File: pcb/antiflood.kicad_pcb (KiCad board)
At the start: 2 copper layers, 88 x 84 mm, 98 parts, among them J1 Barrel_Jack, J10 Screw_Terminal_01x02, J11 Screw_Terminal_01x02, J12 Screw_Terminal_01x02, J13 Screw_Terminal_01x02, J2 Conn_01x03_Male, J3 01x03, J4 01x03, J5 Conn_02x04_Odd_Even, J6 Conn_02x05_Odd_Even, J7 Conn_02x03_Odd_Even, J8 Screw_Terminal_01x02, J9 Screw_Terminal_01x02, K1 P-5, K2 P-5, Q1 MMBT3904, Q2 MMBT3904, SW1 SW_Push, SW2 SW_Push, SW3 SW_Push, U1 ATMEGA328P-AU, U2 TL7705, U3 LM1117-3.3, U4 MT3608, U5 MC34063, U6 TP4056, Y1 16MHz

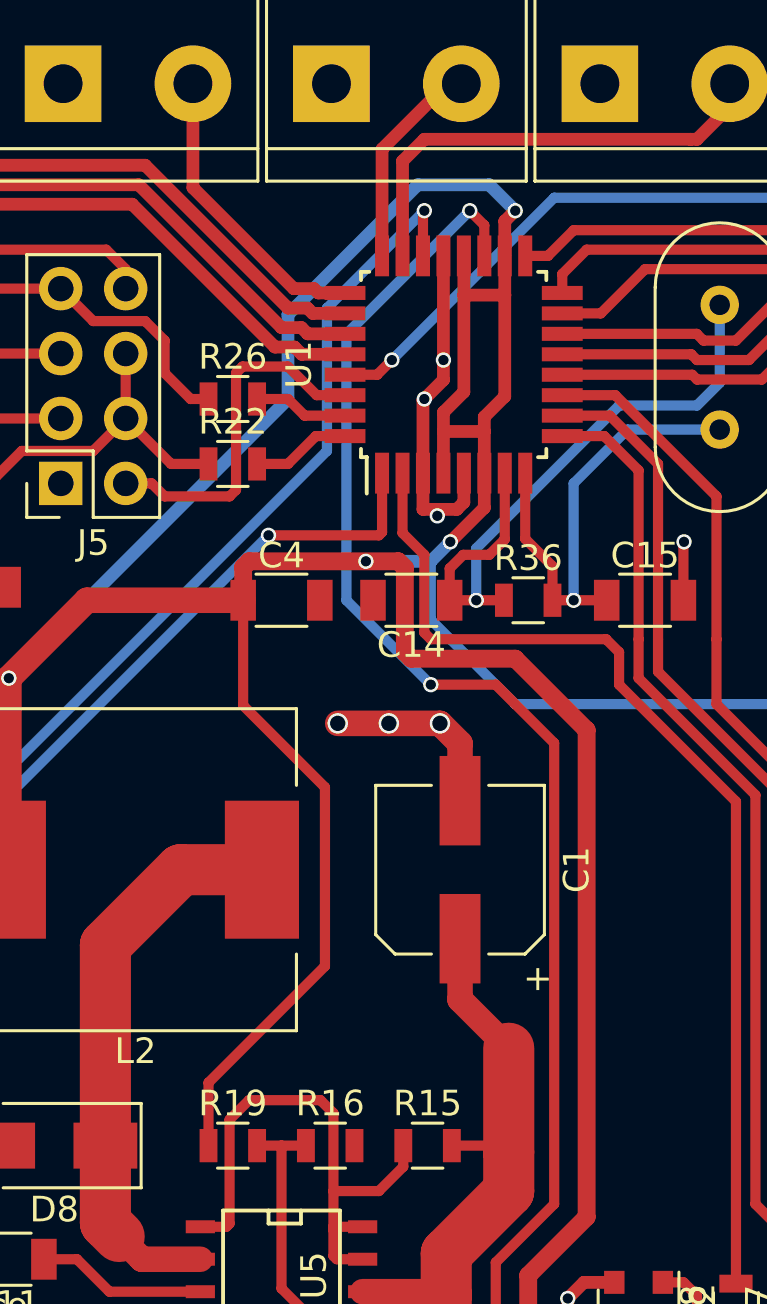
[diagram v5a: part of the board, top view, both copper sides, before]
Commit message: PCB: filled zones
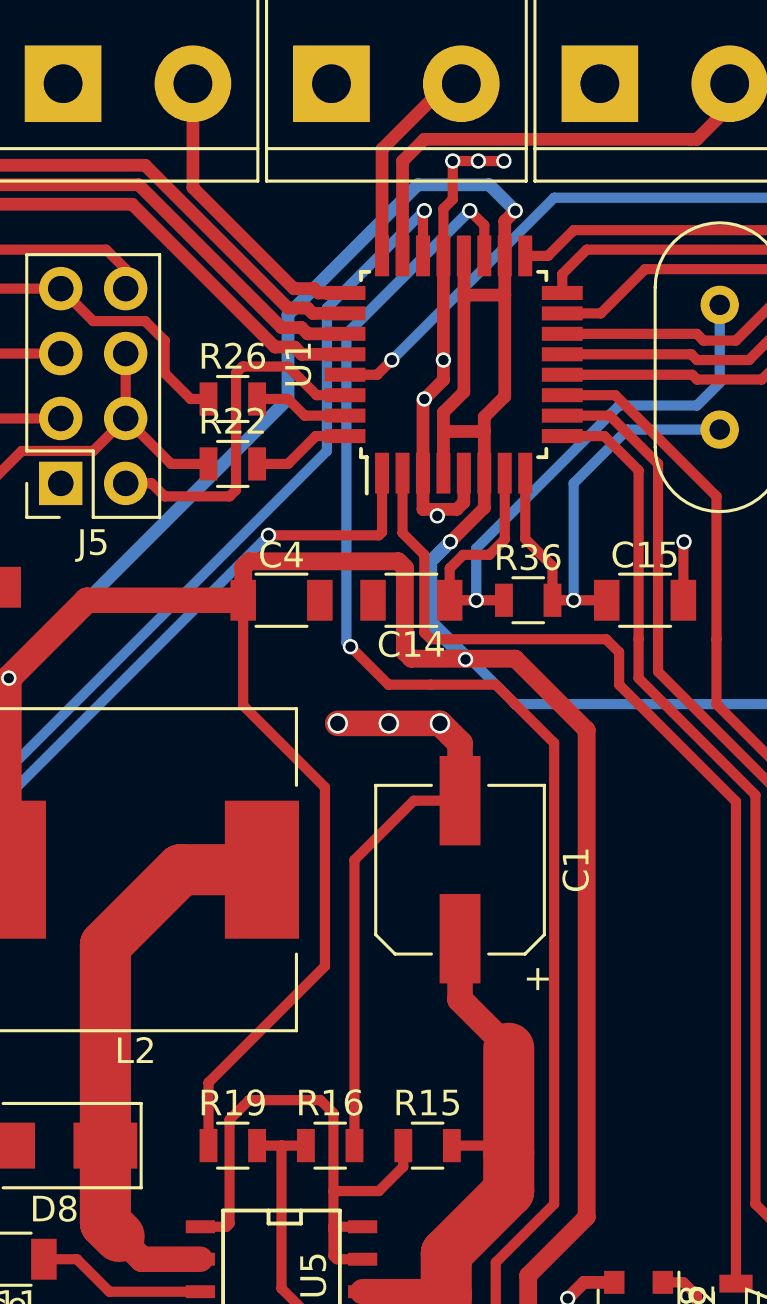
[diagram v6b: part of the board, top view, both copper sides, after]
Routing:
- net GND: track 101.8 -> 123.9 mm, vias 44 -> 47
- net /A6: track 151.7 -> 159.5 mm
- net +5V: track 364.9 -> 363.4 mm
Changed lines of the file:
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@@
   (general
     (links 217)
-    (no_connects 61)
+    (no_connects 0)
     (area 71.454999 50.924999 159.555001 135.025001)
     (thickness 1.6)
     (drawings 24)
-    (tracks 826)
+    (tracks 845)
     (zones 0)
     (modules 98)
@@
     (pad_to_mask_clearance 0)
     (aux_axis_origin 71.505 50.975)
-    (visible_elements FFFEFF7F)
+    (visible_elements FFFEF77F)
     (pcbplotparams
       (layerselection 0x00030_80000001)
@@
   (gr_line (start 159.505 50.975) (end 159.505 134.975) (angle 90) (layer Edge.Cuts) (width 0.1))
   (gr_line (start 71.505 50.975) (end 159.505 50.975) (angle 90) (layer Edge.Cuts) (width 0.1))
+  (segment (start 117.155 96.52) (end 117.155 85.345) (width 0.4) (layer F.Cu) (net 1) (status 400000))
+  (segment (start 119.475 83.025) (end 121.285 83.025) (width 0.4) (layer F.Cu) (net 1) (status 800000))
+  (segment (start 117.155 85.345) (end 119.475 83.025) (width 0.4) (layer F.Cu) (net 1))
+  (segment (start 122 58) (end 123 58) (width 0.4) (layer F.Cu) (net 1))
+  (via (at 123 58) (size 0.6) (drill 0.4) (layers F.Cu B.Cu) (net 1))
+  (segment (start 121 58) (end 122 58) (width 0.4) (layer F.Cu) (net 1))
+  (via (at 122 58) (size 0.6) (drill 0.4) (layers F.Cu B.Cu) (net 1))
+  (segment (start 121 59.5) (end 121 58) (width 0.4) (layer F.Cu) (net 1))
+  (via (at 121 58) (size 0.6) (drill 0.4) (layers F.Cu B.Cu) (net 1))
+  (segment (start 120.635 61.711) (end 120.635 59.865) (width 0.4) (layer F.Cu) (net 1))
+  (segment (start 120.635 59.865) (end 121 59.5) (width 0.4) (layer F.Cu) (net 1))
   (segment (start 100.5 131) (end 100.5 129.5) (width 0.4) (layer F.Cu) (net 1))
   (via (at 100.5 129.5) (size 0.6) (drill 0.4) (layers F.Cu B.Cu) (net 1))
   (segment (start 100.5 132.5) (end 100.5 131) (width 0.4) (layer F.Cu) (net 1))
   (via (at 100.5 131) (size 0.6) (drill 0.4) (layers F.Cu B.Cu) (net 1))
-  (segment (start 102.87 133.095) (end 101.095 133.095) (width 0.4) (layer F.Cu) (net 1) (status 400000))
+  (segment (start 102.87 133.095) (end 101.095 133.095) (width 0.4) (layer F.Cu) (net 1))
   (segment (start 101.095 133.095) (end 100.5 132.5) (width 0.4) (layer F.Cu) (net 1))
   (via (at 100.5 132.5) (size 0.6) (drill 0.4) (layers F.Cu B.Cu) (net 1))
-  (segment (start 84.455 99.06) (end 84.455 98.455) (width 0.5) (layer F.Cu) (net 1) (status 400000))
+  (segment (start 84.455 99.06) (end 84.455 98.455) (width 0.5) (layer F.Cu) (net 1))
   (segment (start 84.455 98.455) (end 83.5 97.5) (width 0.5) (layer F.Cu) (net 1))
   (via (at 83.5 97.5) (size 0.6) (drill 0.4) (layers F.Cu B.Cu) (net 1))
-  (segment (start 76.2 99.06) (end 76.2 98.2) (width 0.5) (layer F.Cu) (net 1) (status 400000))
+  (segment (start 76.2 99.06) (end 76.2 98.2) (width 0.5) (layer F.Cu) (net 1))
   (segment (start 76.2 98.2) (end 75.5 97.5) (width 0.5) (layer F.Cu) (net 1))
   (via (at 75.5 97.5) (size 0.6) (drill 0.4) (layers F.Cu B.Cu) (net 1))
@@
   (segment (start 150.5 104.5) (end 150.5 102.5) (width 1) (layer F.Cu) (net 1))
   (via (at 150.5 102.5) (size 0.8) (drill 0.6) (layers F.Cu B.Cu) (net 1))
-  (segment (start 150.495 106.77) (end 150.495 104.505) (width 1) (layer F.Cu) (net 1) (status 400000))
+  (segment (start 150.495 106.77) (end 150.495 104.505) (width 1) (layer F.Cu) (net 1))
   (segment (start 150.495 104.505) (end 150.5 104.5) (width 1) (layer F.Cu) (net 1))
   (via (at 150.5 104.5) (size 0.8) (drill 0.6) (layers F.Cu B.Cu) (net 1))
@@
   (segment (start 155.5 104.5) (end 155.5 102.5) (width 1) (layer F.Cu) (net 1))
   (via (at 155.5 102.5) (size 0.8) (drill 0.6) (layers F.Cu B.Cu) (net 1))
-  (segment (start 155.575 106.77) (end 155.575 104.575) (width 1) (layer F.Cu) (net 1) (status 400000))
+  (segment (start 155.575 106.77) (end 155.575 104.575) (width 1) (layer F.Cu) (net 1))
   (segment (start 155.575 104.575) (end 155.5 104.5) (width 1) (layer F.Cu) (net 1))
   (via (at 155.5 104.5) (size 0.8) (drill 0.6) (layers F.Cu B.Cu) (net 1))
@@
   (segment (start 109.5 103.5) (end 107.5 103.5) (width 1) (layer F.Cu) (net 1))
   (via (at 107.5 103.5) (size 0.8) (drill 0.6) (layers F.Cu B.Cu) (net 1))
-  (segment (start 111.125 103.505) (end 109.505 103.505) (width 1) (layer F.Cu) (net 1) (status 400000))
+  (segment (start 111.125 103.505) (end 109.505 103.505) (width 1) (layer F.Cu) (net 1))
   (segment (start 109.505 103.505) (end 109.5 103.5) (width 1) (layer F.Cu) (net 1))
   (via (at 109.5 103.5) (size 0.8) (drill 0.6) (layers F.Cu B.Cu) (net 1))
@@
   (segment (start 124.079 121.285) (end 126.365 121.285) (width 2) (layer F.Cu) (net 2))
   (segment (start 120.745 117.951) (end 124.079 121.285) (width 2) (layer F.Cu) (net 2))
+  (segment (start 120.904 72.898) (end 120.142 73.66) (width 0.5) (layer B.Cu) (net 3))
+  (segment (start 120.142 73.66) (end 120.142 76.142) (width 0.5) (layer B.Cu) (net 3))
+  (segment (start 120.142 76.142) (end 121.5 77.5) (width 0.5) (layer B.Cu) (net 3))
+  (via (at 121.5 77.5) (size 0.6) (drill 0.4) (layers F.Cu B.Cu) (net 3))
+  (segment (start 121.5 77.5) (end 121.5 77.47) (width 0.5) (layer F.Cu) (net 3))
+  (segment (start 121.5 77.47) (end 121.5 77.5) (width 0.5) (layer F.Cu) (net 3))
+  (segment (start 121.5 77.5) (end 121.5 77.47) (width 0.5) (layer F.Cu) (net 3))
   (segment (start 112.8 75.184) (end 112.8 79.3) (width 0.4) (layer F.Cu) (net 3))
   (segment (start 112.8 79.3) (end 116 82.5) (width 0.4) (layer F.Cu) (net 3))
@@
   (segment (start 72.136 132.334) (end 72.897 133.095) (width 0.4) (layer F.Cu) (net 3))
   (segment (start 72.897 133.095) (end 77.47 133.095) (width 0.4) (layer F.Cu) (net 3))
-  (segment (start 123.444 77.47) (end 119.38 77.47) (width 0.7) (layer F.Cu) (net 3))
+  (segment (start 123.444 77.47) (end 121.5 77.47) (width 0.7) (layer F.Cu) (net 3))
+  (segment (start 121.5 77.47) (end 119.38 77.47) (width 0.7) (layer F.Cu) (net 3))
   (segment (start 119.38 77.47) (end 119.126 77.216) (width 0.7) (layer F.Cu) (net 3))
   (segment (start 119.126 77.216) (end 119.126 73.914) (width 0.7) (layer F.Cu) (net 3))
@@
   (segment (start 112.8 73.89) (end 112.8 75.184) (width 0.5) (layer F.Cu) (net 3))
   (segment (start 113.03 73.66) (end 112.8 73.89) (width 0.5) (layer F.Cu) (net 3))
-  (segment (start 117.602 73.66) (end 113.03 73.66) (width 0.5) (layer F.Cu) (net 3))
-  (via (at 117.602 73.66) (size 0.6) (drill 0.4) (layers F.Cu B.Cu) (net 3))
-  (segment (start 120.142 73.66) (end 117.602 73.66) (width 0.5) (layer B.Cu) (net 3))
   (segment (start 120.904 72.898) (end 120.142 73.66) (width 0.5) (layer B.Cu) (net 3))
   (via (at 120.904 72.898) (size 0.6) (drill 0.4) (layers F.Cu B.Cu) (net 3))
@@
   (segment (start 114.554 66.04) (end 112.776 66.04) (width 0.4) (layer F.Cu) (net 11))
   (segment (start 115.675 67.161) (end 114.554 66.04) (width 0.4) (layer F.Cu) (net 11))
+  (segment (start 120.142 78.486) (end 118.486 78.486) (width 0.4) (layer F.Cu) (net 12))
+  (segment (start 118.486 78.486) (end 117 77) (width 0.4) (layer F.Cu) (net 12))
+  (via (at 117 77) (size 0.6) (drill 0.4) (layers F.Cu B.Cu) (net 12))
+  (segment (start 117 77) (end 116.84 76.84) (width 0.4) (layer B.Cu) (net 12))
+  (segment (start 116.84 76.84) (end 116.84 64.77) (width 0.4) (layer B.Cu) (net 12))
+  (segment (start 116.84 64.77) (end 121.666 59.944) (width 0.4) (layer B.Cu) (net 12))
   (segment (start 124.968 98.806) (end 124.968 80.772) (width 0.4) (layer F.Cu) (net 12))
   (segment (start 124.968 80.772) (end 122.682 78.486) (width 0.4) (layer F.Cu) (net 12))
   (segment (start 122.682 78.486) (end 120.142 78.486) (width 0.4) (layer F.Cu) (net 12))
-  (via (at 120.142 78.486) (size 0.6) (drill 0.4) (layers F.Cu B.Cu) (net 12))
-  (segment (start 120.142 78.486) (end 116.84 75.184) (width 0.4) (layer B.Cu) (net 12))
-  (segment (start 116.84 75.184) (end 116.84 64.77) (width 0.4) (layer B.Cu) (net 12))
   (segment (start 116.84 64.77) (end 121.666 59.944) (width 0.4) (layer B.Cu) (net 12))
   (via (at 121.666 59.944) (size 0.6) (drill 0.4) (layers F.Cu B.Cu) (net 12))
@@
     (connect_pads (clearance 0.508))
     (min_thickness 0.254)
-    (fill (arc_segments 16) (thermal_gap 0.508) (thermal_bridge_width 0.508) (smoothing fillet) (radius 0.508))
+    (fill yes (arc_segments 16) (thermal_gap 0.508) (thermal_bridge_width 0.508) (smoothing fillet) (radius 0.508))
     (polygon
       (pts
@@
     (connect_pads (clearance 0.508))
     (min_thickness 0.254)
-    (fill (arc_segments 16) (thermal_gap 0.508) (thermal_bridge_width 0.508) (smoothing fillet) (radius 0.508))
+    (fill yes (arc_segments 16) (thermal_gap 0.508) (thermal_bridge_width 0.508) (smoothing fillet) (radius 0.508))
     (polygon
       (pts

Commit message: PCB: references
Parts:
- renumbered D9 to ?, R33 to ?, R34 to ?, R35 to ?, REF** to ?, D10 to ?, D11 to ?, D12 to ?, R30 to ?, R31 to ?, R32 to ?, D13 to ?, D14 to ?
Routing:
- net +3V3: track 64.5 -> 68.6 mm
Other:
- board text added: "D14-D9"
- board text added: "R35-R30"

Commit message: PB: text
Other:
- board text added: "+"
- board text added: "-"
- board text added: "3.7 V"
- board text added: "ESP01"
- board text added: "ICSP"
- board text added: "Li-Ion"
- board text added: "MISO SCK RST"
- board text added: "MOSI DBG RST SCK MISO"
- board text added: "Vcc GND GND GND GND"
- board text added: "Vcc MOSI GND"
- board text added: "WiFi Antenna"
- board text added: "t°"
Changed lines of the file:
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@@
     (area 68.157143 48.874999 162.842858 137.075001)
     (thickness 1.6)
-    (drawings 26)
+    (drawings 49)
     (tracks 845)
     (zones 0)
@@
     (39 F.Mask user)
     (40 Dwgs.User user)
-    (41 Cmts.User user)
+    (41 Cmts.User user hide)
     (42 Eco1.User user hide)
     (43 Eco2.User user hide)
@@
     (descr "Through hole straight socket strip, 2x05, 2.54mm pitch, double rows")
     (tags "Through hole socket strip THT 2x05 2.54mm double row")
-    (fp_text reference J6 (at -5.207 5.588 180) (layer F.SilkS)
+    (fp_text reference J6 (at -5.207 2.413 180) (layer F.SilkS)
       (effects (font (size 1 1) (thickness 0.15)))
     )
@@
     (descr "Through hole straight socket strip, 2x03, 2.54mm pitch, double rows")
     (tags "Through hole socket strip THT 2x03 2.54mm double row")
-    (fp_text reference J7 (at -4.826 3.048 180) (layer F.SilkS)
+    (fp_text reference J7 (at -4.826 1.143 180) (layer F.SilkS)
       (effects (font (size 1 1) (thickness 0.15)))
     )
@@
     (pad 1 thru_hole circle (at 0 0) (size 6.4 6.4) (drill 3.2) (layers *.Cu *.Mask))
   )
+  (gr_text "3.7 V" (at 82.804 124.968) (layer Dwgs.User)
+    (effects (font (size 1.5 1.5) (thickness 0.3)))
+  )
+  (gr_text Li-Ion (at 82.804 122.428) (layer Dwgs.User)
+    (effects (font (size 1.5 1.5) (thickness 0.3)))
+  )
+  (gr_text - (at 90.932 122.936) (layer Dwgs.User)
+    (effects (font (size 1.5 1.5) (thickness 0.3)))
+  )
+  (gr_text t° (at 91.44 120.396) (layer Dwgs.User)
+    (effects (font (size 1.5 1.5) (thickness 0.3)))
+  )
+  (gr_text + (at 90.932 117.856) (layer Dwgs.User)
+    (effects (font (size 1.5 1.5) (thickness 0.3)))
+  )
+  (gr_text "WiFi\nAntenna" (at 91.44 66.548) (layer Dwgs.User)
+    (effects (font (size 1.5 1.5) (thickness 0.3)))
+  )
+  (gr_line (start 150.876 80.772) (end 150.876 81.28) (angle 90) (layer Dwgs.User) (width 0.2))
+  (gr_line (start 151.384 80.264) (end 150.876 80.772) (angle 90) (layer Dwgs.User) (width 0.2))
+  (gr_line (start 154.432 70.104) (end 153.924 70.612) (angle 90) (layer Dwgs.User) (width 0.2))
+  (gr_line (start 150.876 87.376) (end 150.876 81.28) (angle 90) (layer Dwgs.User) (width 0.2))
+  (gr_line (start 159.004 87.376) (end 150.876 87.376) (angle 90) (layer Dwgs.User) (width 0.2))
+  (gr_line (start 159.004 80.264) (end 159.004 87.376) (angle 90) (layer Dwgs.User) (width 0.2))
+  (gr_line (start 151.384 80.264) (end 159.004 80.264) (angle 90) (layer Dwgs.User) (width 0.2))
+  (gr_line (start 153.924 78.232) (end 153.924 70.612) (angle 90) (layer Dwgs.User) (width 0.2))
+  (gr_line (start 159.004 78.232) (end 153.924 78.232) (angle 90) (layer Dwgs.User) (width 0.2))
+  (gr_line (start 159.004 70.104) (end 159.004 78.232) (angle 90) (layer Dwgs.User) (width 0.2))
+  (gr_line (start 154.432 70.104) (end 159.004 70.104) (angle 90) (layer Dwgs.User) (width 0.2))
+  (gr_text "Vcc\nGND\nGND\nGND\nGND" (at 154.94 85.852 90) (layer Dwgs.User)
+    (effects (font (size 1 1) (thickness 0.153)))
+  )
+  (gr_text "MOSI\nDBG\nRST\nSCK\nMISO" (at 154.94 82.296 90) (layer Dwgs.User)
+    (effects (font (size 1 1) (thickness 0.153)))
+  )
+  (gr_text "Vcc\nMOSI\nGND" (at 156.464 76.2 90) (layer Dwgs.User)
+    (effects (font (size 1 1) (thickness 0.153)))
+  )
+  (gr_text "MISO\nSCK\nRST" (at 156.464 72.136 90) (layer Dwgs.User)
+    (effects (font (size 1 1) (thickness 0.153)))
+  )
+  (gr_text ICSP (at 148.844 73.152) (layer Dwgs.User)
+    (effects (font (size 1.5 1.5) (thickness 0.3)))
+  )
+  (gr_text ESP01 (at 108.712 75.184) (layer Dwgs.User)
+    (effects (font (size 1.5 1.5) (thickness 0.3)))
+  )
   (gr_text R35-R30 (at 146.685 62.865) (layer F.SilkS)
     (effects (font (size 1 1) (thickness 0.15)))
@@
   (segment (start 92.743 83.025) (end 89.295 86.473) (width 1.5) (layer F.Cu) (net 3))
   (segment (start 89.295 86.473) (end 89.295 88.875) (width 1.5) (layer F.Cu) (net 3))
-  (segment (start 99.314 68.072) (end 100.65 68.072) (width 0.4) (layer F.Cu) (net 4) (status 800000))
-  (segment (start 99.314 65.532) (end 100.65 65.532) (width 0.4) (layer F.Cu) (net 4) (status 800000))
+  (segment (start 99.314 68.072) (end 100.65 68.072) (width 0.4) (layer F.Cu) (net 4))
+  (segment (start 99.314 65.532) (end 100.65 65.532) (width 0.4) (layer F.Cu) (net 4))
   (segment (start 107.442 61.214) (end 108.204 61.976) (width 0.7) (layer F.Cu) (net 4))
   (segment (start 99.568 74.676) (end 99.314 74.422) (width 0.7) (layer F.Cu) (net 4))
@@
   (segment (start 99.314 61.722) (end 99.822 61.214) (width 0.7) (layer F.Cu) (net 4))
   (segment (start 99.822 61.214) (end 107.442 61.214) (width 0.7) (layer F.Cu) (net 4))
-  (segment (start 100.608 74.676) (end 99.568 74.676) (width 0.7) (layer F.Cu) (net 4) (status 400000))
-  (segment (start 108.204 61.976) (end 108.204 62.992) (width 0.7) (layer F.Cu) (net 4) (status 800000))
+  (segment (start 100.608 74.676) (end 99.568 74.676) (width 0.7) (layer F.Cu) (net 4))
+  (segment (start 108.204 61.976) (end 108.204 62.992) (width 0.7) (layer F.Cu) (net 4))
   (segment (start 86.995 82.575) (end 86.995 78.74) (width 1) (layer F.Cu) (net 4))
   (segment (start 86.995 78.74) (end 87.122 78.867) (width 1) (layer F.Cu) (net 4))
